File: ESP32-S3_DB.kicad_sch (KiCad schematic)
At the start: 0 parts

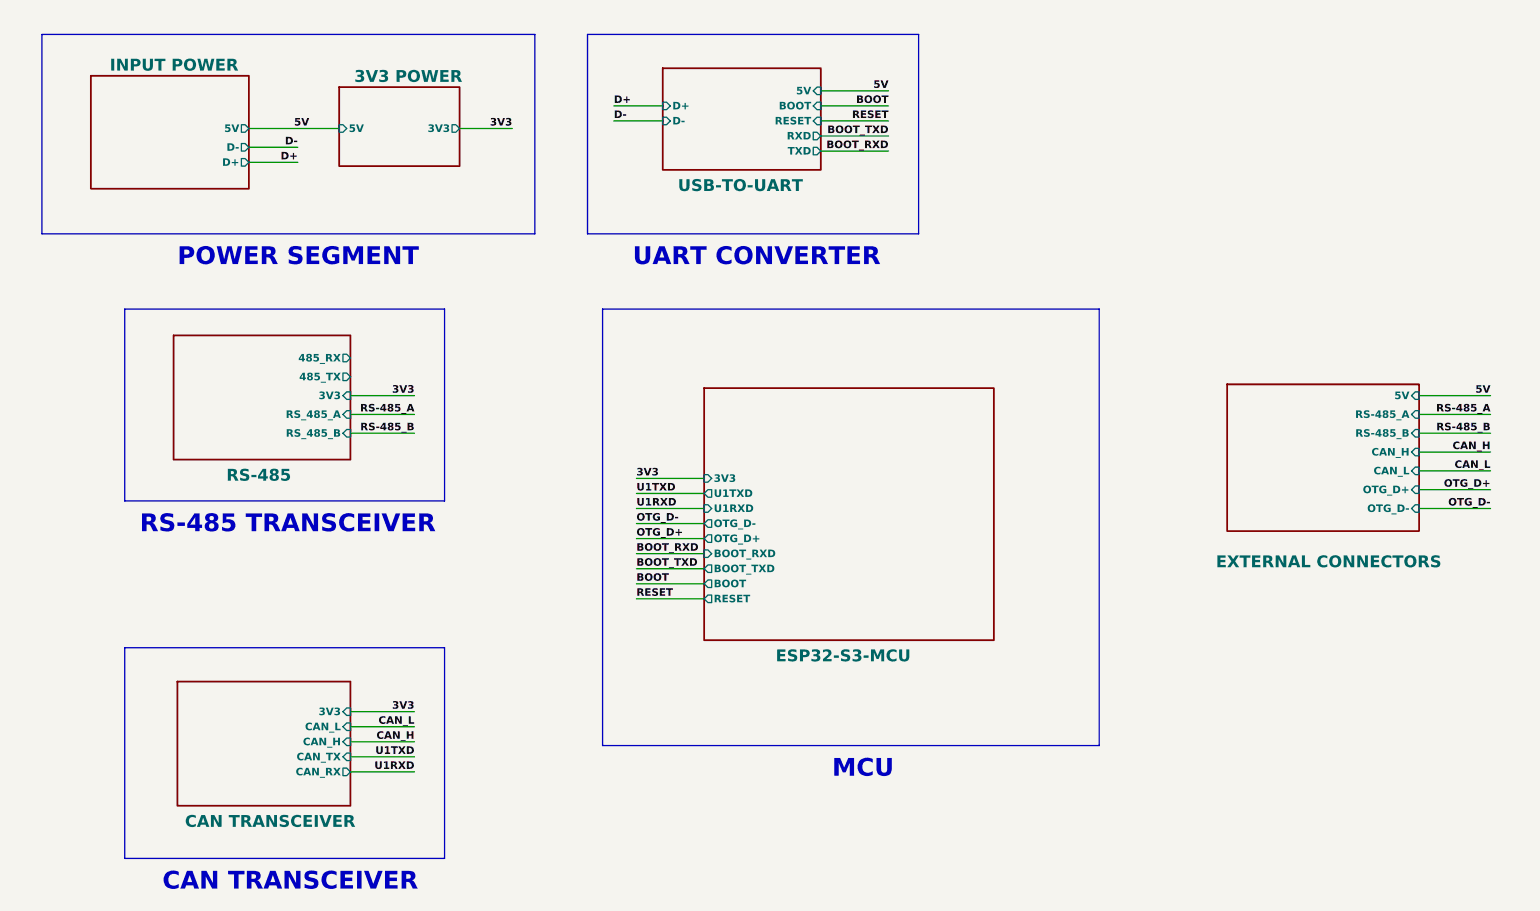
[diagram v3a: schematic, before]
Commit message: Assigned UART port 2 for RS-485
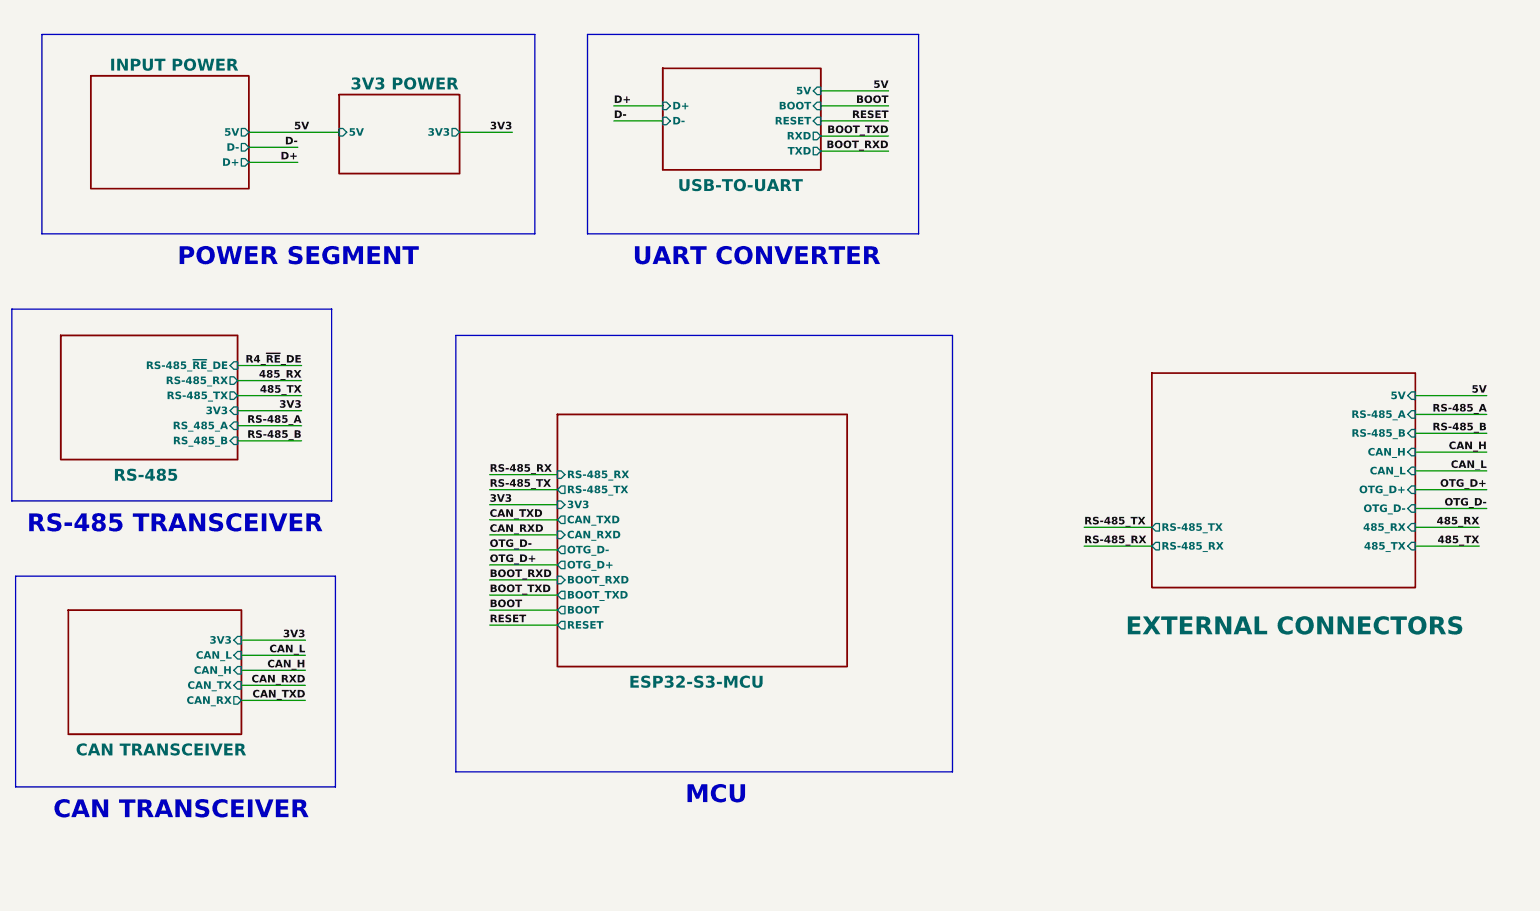
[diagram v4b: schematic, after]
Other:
- sheet ESP32-S3-MCU ports: added CAN_RXD, CAN_TXD, RS-485_RX, RS-485_TX; removed U1RXD, U1TXD
- sheet EXTERNAL CONNECTORS ports: added 485_RX, 485_TX, RS-485_RX, RS-485_TX; removed none
- sheet RS-485 ports: added RS-485_RX, RS-485_TX, RS-485_~{RE}_DE; removed 485_RX, 485_TX

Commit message: Added SD card interface
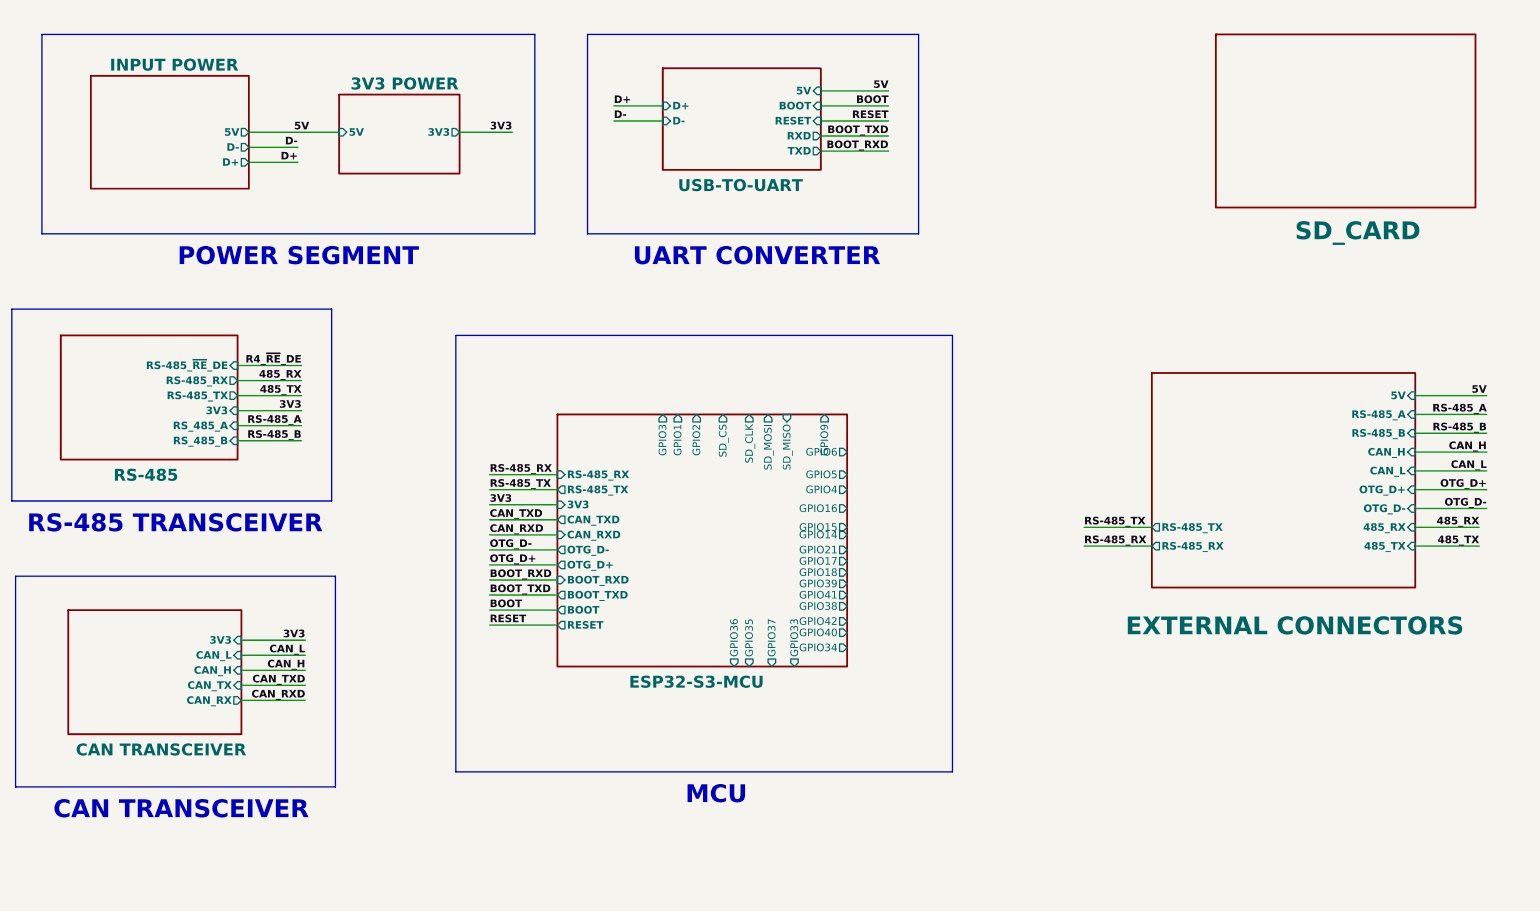
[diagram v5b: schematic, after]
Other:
- added sheet SD_CARD (SD_Card.kicad_sch)
- sheet ESP32-S3-MCU ports: added GPIO1, GPIO14, GPIO15, GPIO16, GPIO17, GPIO18, GPIO2, GPIO21, GPIO3, GPIO33, GPIO34, GPIO35, GPIO36, GPIO37, GPIO38, GPIO39, GPIO4, GPIO40, GPIO41, GPIO42, GPIO5, GPIO6, GPIO9, SD_CLK, SD_CS, SD_MISO, SD_MOSI; removed none
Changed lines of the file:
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@@
     (effects (font (size 1.27 1.27) bold (color 255 0 0 1)) (justify left bottom))
   )
-  (label "CAN_TXD" (at 71.12 133.985 180) (fields_autoplaced)
+  (label "CAN_TXD" (at 71.12 131.445 180) (fields_autoplaced)
     (effects (font (size 1.27 1.27) bold (color 0 0 255 1)) (justify right bottom))
   )
@@
     (effects (font (size 1.27 1.27) bold (color 0 0 255 1)) (justify right bottom))
   )
-  (label "CAN_RXD" (at 71.12 131.445 180) (fields_autoplaced)
+  (label "CAN_RXD" (at 71.12 133.985 180) (fields_autoplaced)
     (effects (font (size 1.27 1.27) bold (color 0 0 255 1)) (justify right bottom))
   )
@@
     (effects (font (size 1.27 1.27) bold (color 0 0 0 1)) (justify right bottom))
   )
+  (sheet (at 224.79 21.59) (size 43.815 29.21)
+    (stroke (width 0.3) (type solid) (color 0 0 0 1))
+    (fill (color 255 255 194 1.0000))
+    (property "Sheetname" "SD_CARD" (at 238.125 56.515 0)
+      (effects (font (size 3 3) bold (color 255 0 0 1)) (justify left bottom))
+    )
+    (property "Sheetfile" "SD_Card.kicad_sch" (at 224.79 51.3846 0)
+      (effects (font (size 1.27 1.27)) (justify left top) hide)
+    )
+    (instances
+      (project "ESP32-S3_DB"
+        (path "/b7fc4bd3-c219-4455-832b-8d795385dcf1" (page "9"))
+      )
+    )
+  )
   (sheet (at 31.115 118.745) (size 29.21 20.955)
     (stroke (width 0.3) (type solid) (color 0 0 0 1))
@@
       (effects (font (size 1.27 1.27) (thickness 0.254) bold (color 0 0 255 1)) (justify left))
     )
-    (instances
+    (pin "GPIO3" output (at 131.445 85.725 90)
+      (effects (font (size 1.27 1.27)) (justify right))
+    )
+    (pin "GPIO1" output (at 133.985 85.725 90)
+      (effects (font (size 1.27 1.27)) (justify right))
+    )
+    (pin "GPIO2" output (at 137.16 85.725 90)
+      (effects (font (size 1.27 1.27)) (justify right))
+    )
+    (pin "SD_CS" output (at 141.605 85.725 90)
+      (effects (font (size 1.27 1.27)) (justify right))
+    )
+    (pin "SD_CLK" output (at 146.05 85.725 90)
+      (effects (font (size 1.27 1.27)) (justify right))
+    )
+    (pin "SD_MOSI" output (at 149.225 85.725 90)
+      (effects (font (size 1.27 1.27)) (justify right))
+    )
+    (pin "SD_MISO" input (at 152.4 85.725 90)
+      (effects (font (size 1.27 1.27)) (justify right))
+    )
+    (pin "GPIO9" output (at 158.75 85.725 90)
+      (effects (font (size 1.27 1.27)) (justify right))
+    )
+    (pin "GPIO6" output (at 162.56 92.075 0)
+      (effects (font (size 1.27 1.27)) (justify right))
+    )
+    (pin "GPIO5" output (at 162.56 95.885 0)
+      (effects (font (size 1.27 1.27)) (justify right))
+    )
+    (pin "GPIO4" output (at 162.56 98.425 0)
+      (effects (font (size 1.27 1.27)) (justify right))
+    )
+    (pin "GPIO16" output (at 162.56 101.6 0)
+      (effects (font (size 1.27 1.27)) (justify right))
+    )
+    (pin "GPIO15" output (at 162.56 104.775 0)
+      (effects (font (size 1.27 1.27)) (justify right))
+    )
+    (pin "GPIO14" output (at 162.56 106.045 0)
+      (effects (font (size 1.27 1.27)) (justify right))
+    )
+    (pin "GPIO21" output (at 162.56 108.585 0)
+      (effects (font (size 1.27 1.27)) (justify right))
+    )
+    (pin "GPIO17" output (at 162.56 110.49 0)
+      (effects (font (size 1.27 1.27)) (justify right))
+    )
+    (pin "GPIO18" output (at 162.56 112.395 0)
+      (effects (font (size 1.27 1.27)) (justify right))
+    )
+    (pin "GPIO39" output (at 162.56 114.3 0)
+      (effects (font (size 1.27 1.27)) (justify right))
+    )
+    (pin "GPIO41" output (at 162.56 116.205 0)
+      (effects (font (size 1.27 1.27)) (justify right))
+    )
+    (pin "GPIO38" output (at 162.56 118.11 0)
+      (effects (font (size 1.27 1.27)) (justify right))
+    )
+    (pin "GPIO42" output (at 162.56 120.65 0)
+      (effects (font (size 1.27 1.27)) (justify right))
+    )
+    (pin "GPIO40" output (at 162.56 122.555 0)
+      (effects (font (size 1.27 1.27)) (justify right))
+    )
+    (pin "GPIO34" output (at 162.56 125.095 0)
+      (effects (font (size 1.27 1.27)) (justify right))
+    )
+    (pin "GPIO33" output (at 153.67 128.27 270)
+      (effects (font (size 1.27 1.27)) (justify left))
+    )
+    (pin "GPIO37" output (at 149.86 128.27 270)
+      (effects (font (size 1.27 1.27)) (justify left))
+    )
+    (pin "GPIO35" output (at 146.05 128.27 270)
+      (effects (font (size 1.27 1.27)) (justify left))
+    )
+    (pin "GPIO36" output (at 143.51 128.27 270)
+      (effects (font (size 1.27 1.27)) (justify left))
+    )
+    (instances

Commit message: Added SD card protection
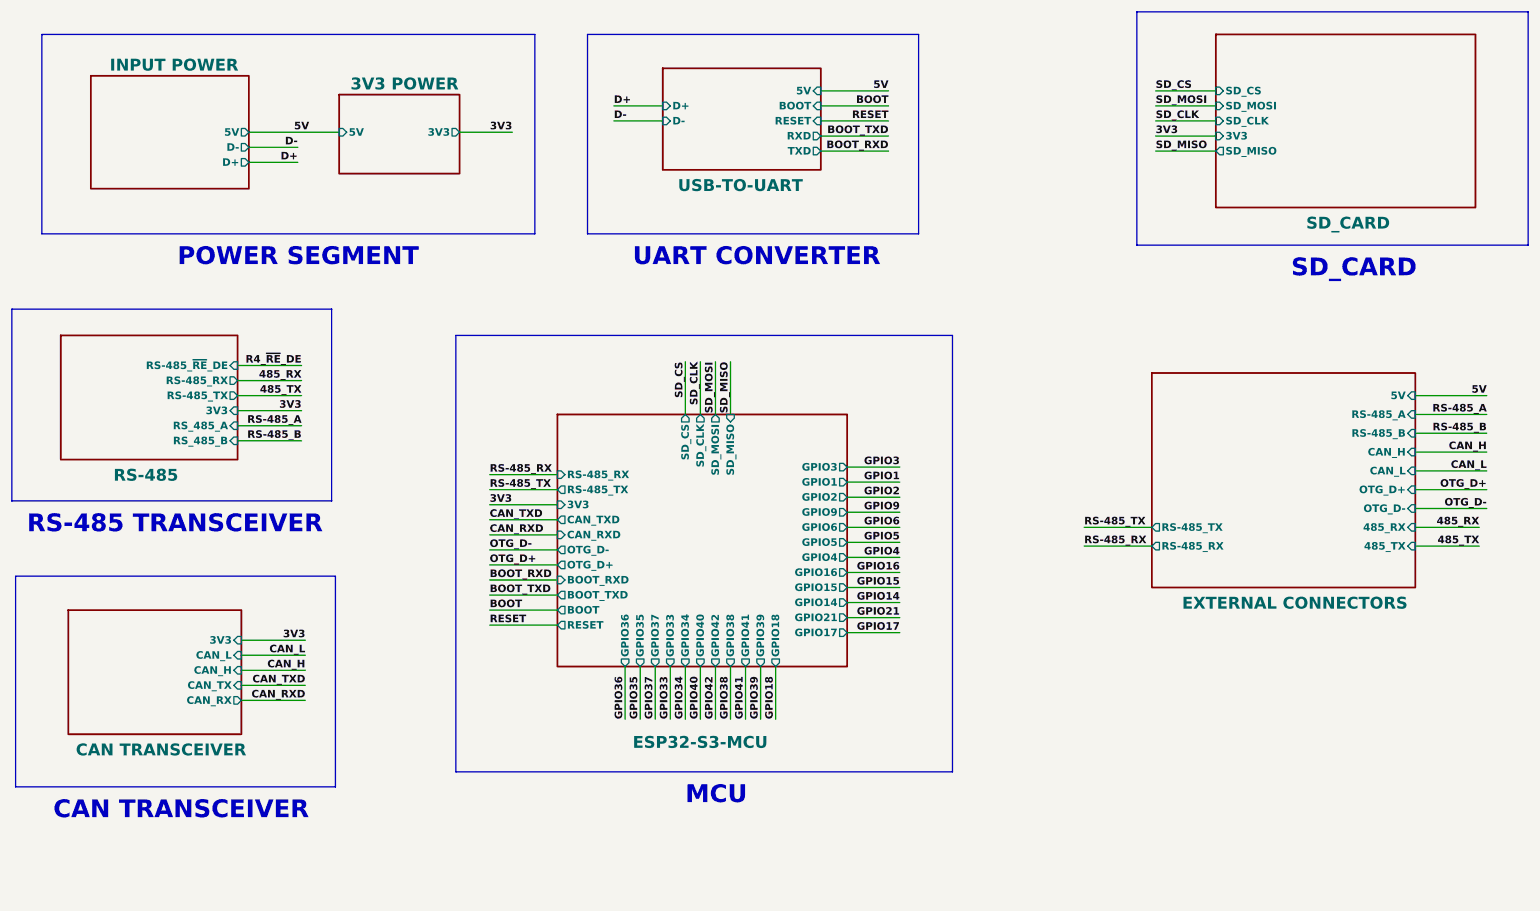
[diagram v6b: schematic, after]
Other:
- sheet SD_CARD ports: added 3V3, SD_CLK, SD_CS, SD_MISO, SD_MOSI; removed none
- note added: "SD_CARD"

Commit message: Added Female Headers
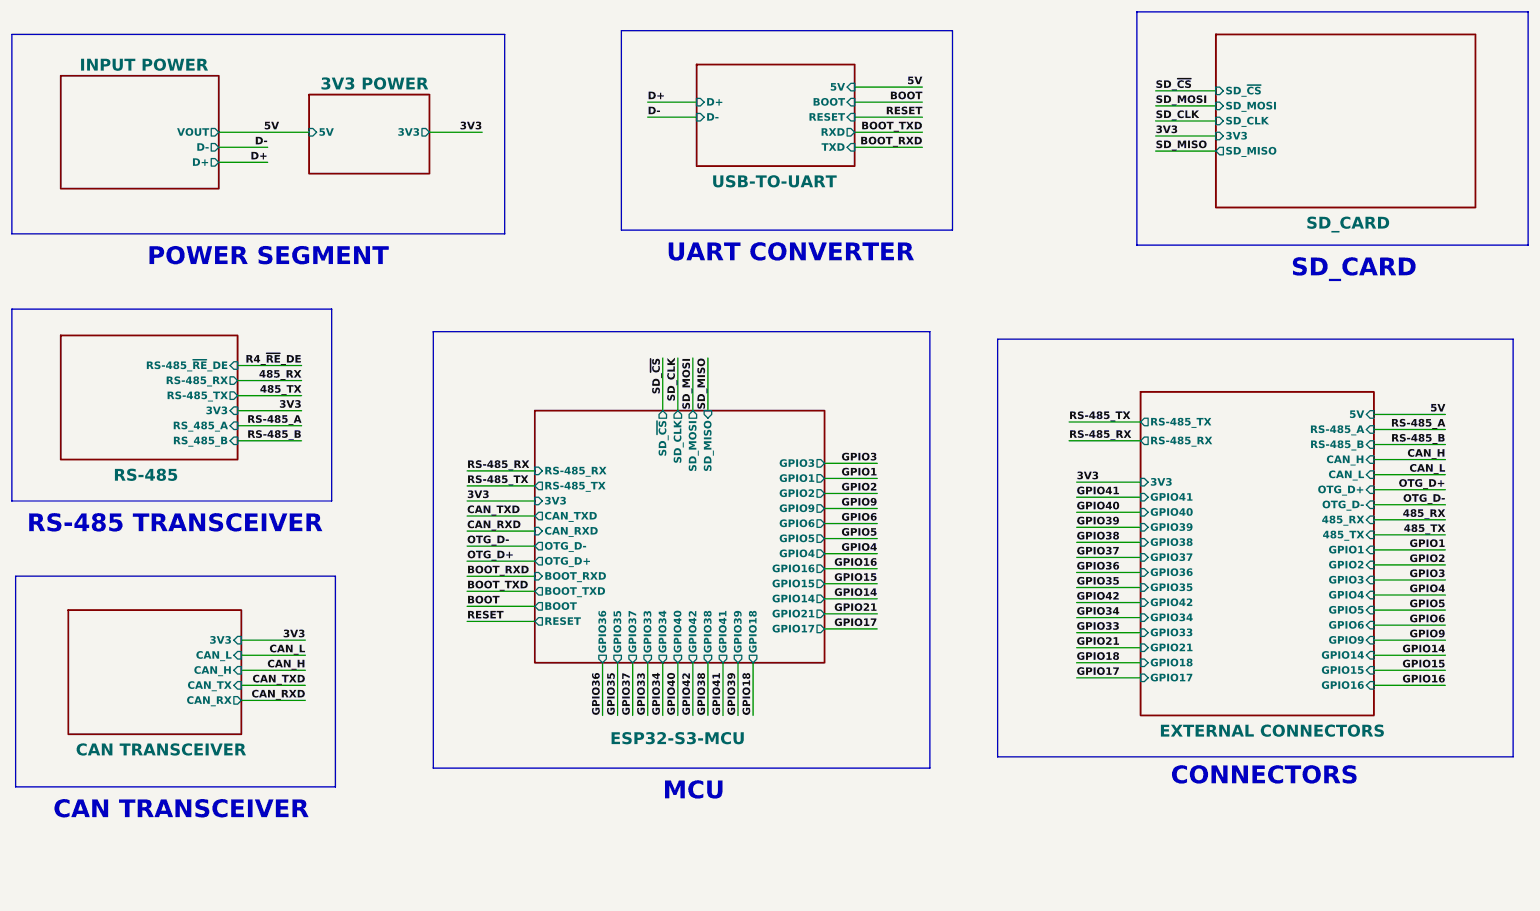
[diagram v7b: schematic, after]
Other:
- sheet ESP32-S3-MCU ports: added SD_~{CS}; removed SD_CS
- sheet EXTERNAL CONNECTORS ports: added 3V3, GPIO1, GPIO14, GPIO15, GPIO16, GPIO17, GPIO18, GPIO2, GPIO21, GPIO3, GPIO33, GPIO34, GPIO35, GPIO36, GPIO37, GPIO38, GPIO39, GPIO4, GPIO40, GPIO41, GPIO42, GPIO5, GPIO6, GPIO9; removed none
- sheet INPUT POWER ports: added VOUT; removed 5V
- sheet SD_CARD ports: added SD_~{CS}; removed SD_CS
- note added: "CONNECTORS"
